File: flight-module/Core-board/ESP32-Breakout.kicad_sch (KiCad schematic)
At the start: 14 parts, among them J3 USB_B_Micro, SW1 SW_MEC_5E, SW2 SW_MEC_5E, U10 ESP32-S3-WROOM-1-N16R2, U9 AZ1084-3.3

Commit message: Finished flight-core.
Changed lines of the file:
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@@
-    (stroke (width 0) (type default))
-  )
-  (wire (pts (xy 205.74 99.06) (xy 205.74 99.822))
     (stroke (width 0) (type default))
   )
@@
     )
   )
-  (symbol (lib_id "power:GND") (at 205.74 99.822 0) (mirror y) (unit 1)
-    (in_bom yes) (on_board yes) (dnp no) (fields_autoplaced)
-    (property "Reference" "#PWR01" (at 205.74 106.172 0)
-      (effects (font (size 1.27 1.27)) hide)
-    )
-    (property "Value" "GND" (at 205.74 103.9575 0)
-      (effects (font (size 1.27 1.27)))
-    )
-    (property "Footprint" "" (at 205.74 99.822 0)
-      (effects (font (size 1.27 1.27)) hide)
-    )
-    (property "Datasheet" "" (at 205.74 99.822 0)
-      (effects (font (size 1.27 1.27)) hide)
-    )
+  (symbol (lib_id "power:GND") (at 205.74 99.06 0) (mirror y) (unit 1)
+    (in_bom yes) (on_board yes) (dnp no) (fields_autoplaced)
+    (property "Reference" "#PWR01" (at 205.74 105.41 0)
+      (effects (font (size 1.27 1.27)) hide)
+    )
+    (property "Value" "GND" (at 205.74 103.1955 0)
+      (effects (font (size 1.27 1.27)))
+    )
+    (property "Footprint" "" (at 205.74 99.06 0)
+      (effects (font (size 1.27 1.27)) hide)
+    )
+    (property "Datasheet" "" (at 205.74 99.06 0)
+      (effects (font (size 1.27 1.27)) hide)
+    )

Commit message: Updated core board.
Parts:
- removed C1 (x2): 1uF, Capacitor_SMD:C_0805_2012Metric_Pad1.18x1.45mm_HandSolder, symbol Device:C
- removed SW1, SW2: SW_MEC_5E, Button_Switch_SMD:SW_SPST_TL3305A, symbol Switch:SW_MEC_5E
- added C1 (x2): 1uF, Capacitor_SMD:C_0805_2012Metric_Pad1.18x1.45mm_HandSolder, symbol Device:C
- added SW1, SW2: 1825910-6, 1825910-6:SW_1825910-6-4, symbol 1825910-6:1825910-6
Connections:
- net BOOT: now also C1.2, SW1.3, SW1.4
- net EN: now also C1.2, SW2.3, SW2.4
- net GND: now also C1.1, C1.1, SW1.1, SW1.2, SW2.1, SW2.2
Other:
- note removed: "Buttons"

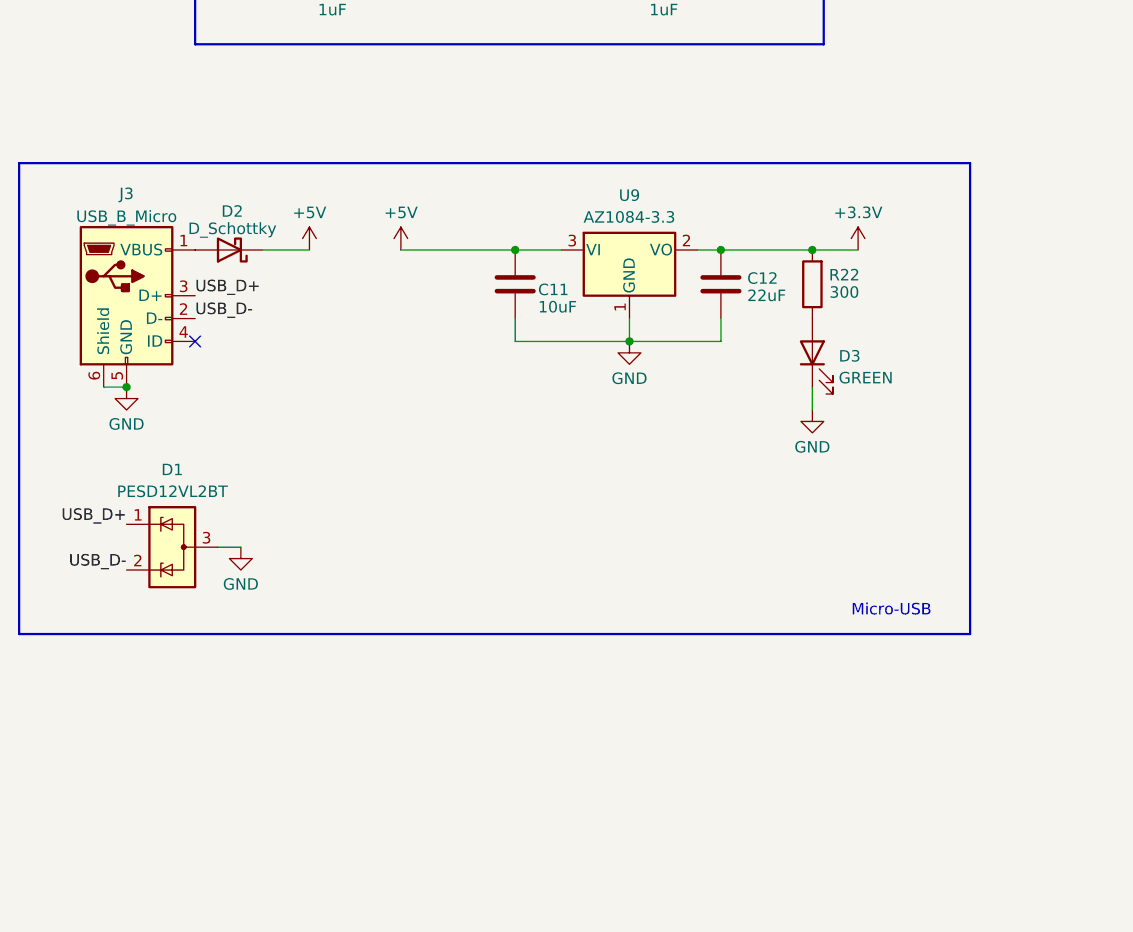
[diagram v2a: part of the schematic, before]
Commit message: Minor changes to footprint library
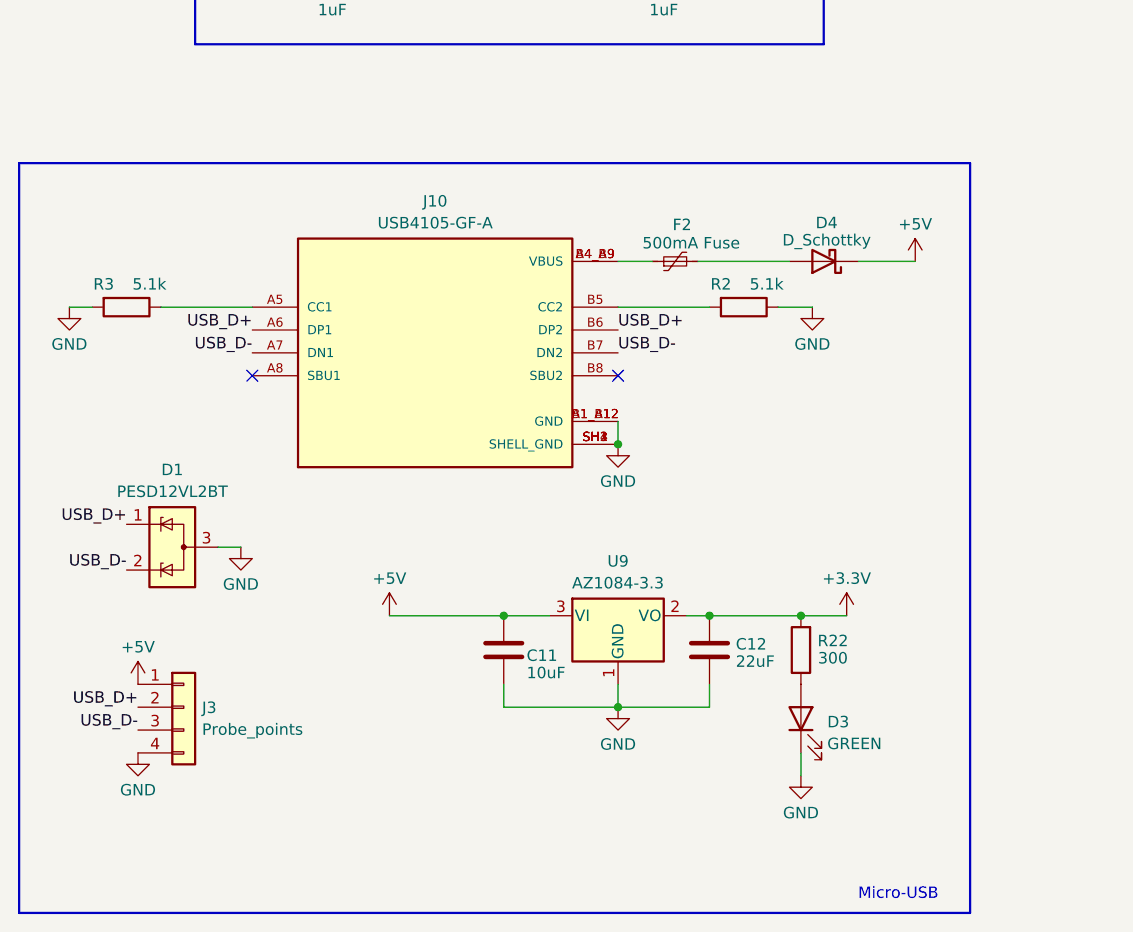
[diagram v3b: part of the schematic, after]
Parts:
- removed D2: D_Schottky, Diode_SMD:D_SOD-128, symbol Device:D_Schottky
- removed J3: USB_B_Micro, Connector_USB:USB_Micro-B_Amphenol_10103594-0001LF_Horizontal, symbol Connector:USB_B_Micro
- added D4: D_Schottky, Diode_SMD:D_SOD-128, symbol Device:D_Schottky
- added F2: 500mA Fuse, Fuse:Fuse_0603_1608Metric, symbol Device:Polyfuse_Small
- added J10: USB4105-GF-A, USB4105-GF-A:GCT_USB4105-GF-A, symbol USB4105-GF-A:USB4105-GF-A
- added J3: Probe_points, Connector_PinHeader_2.54mm:PinHeader_1x04_P2.54mm_Vertical, symbol Connector_Generic:Conn_01x04
- added R2, R3: 5.1k, Resistor_SMD:R_0805_2012Metric_Pad1.20x1.40mm_HandSolder, symbol Device:R
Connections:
- net +5V: now also D4.1 (K), J3.1 (Pin_1)
- net GND: now also J10.A1_B12 (GND), J10.B1_A12 (GND), J10.SH1 (SHELL_GND), J10.SH2 (SHELL_GND), J10.SH3 (SHELL_GND), J10.SH4 (SHELL_GND), J3.4 (Pin_4), R2.1, R3.2
- net USB_D+: now also J10.A6 (DP1), J10.B6 (DP2), J3.2 (Pin_2)
- net USB_D-: now also J10.A7 (DN1), J10.B7 (DN2), J3.3 (Pin_3)
- new net: D4.2 (A), F2.2
- new net: F2.1, J10.A4_B9 (VBUS), J10.B4_A9 (VBUS)
- new net: J10.A5 (CC1), R3.1
- new net: J10.B5 (CC2), R2.2
- no-connect marks 9 -> 10
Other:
- moved on the sheet: C11, C12, D3, R22, U9

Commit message: change the USB layout
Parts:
- J10: footprint USB4105-GF-A:GCT_USB4105-GF-A -> Connector_USB:USB_C_Receptacle_GCT_USB4105-xx-A_16P_TopMnt_Horizontal
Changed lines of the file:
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@@
       (effects (font (size 1.27 1.27)))
     )
-    (property "Footprint" "USB4105-GF-A:GCT_USB4105-GF-A" (at 80.01 100.33 0)
+    (property "Footprint" "Connector_USB:USB_C_Receptacle_GCT_USB4105-xx-A_16P_TopMnt_Horizontal" (at 80.01 100.33 0)
       (effects (font (size 1.27 1.27)) (justify bottom) hide)
     )

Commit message: in the middle of updating micro usb
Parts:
- removed D4: D_Schottky, Diode_SMD:D_SOD-128, symbol Device:D_Schottky
- removed SW1, SW2: 1825910-6, 1825910-6:SW_1825910-6-4, symbol 1825910-6:1825910-6
- added D2: D_Schottky, Diode_SMD:D_SOD-128, symbol Device:D_Schottky
- added J11: 10118194-0011LF, 10118194-0011LF:AMPHENOL_10118194-0011LF, symbol MicroUSB:10118194-0011LF
- added SW1, SW3: SW_SPST, Button_Switch_THT:SW_PUSH_6mm, symbol Switch:SW_SPST
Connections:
- net +5V: now also D2.2 (A)
- net BOOT: now also SW3.2 (B)
- net EN: now also SW1.2 (B)
- net GND: now also SW1.1 (A), SW3.1 (A)
- net USB_D+: now also J11.3 (D+); no longer J10.B6 (DP2)
- net USB_D-: now also J11.2 (D-); no longer J10.B7 (DN2)
- net at F2.2: now also J11.1 (VBUS)
- net at J10.A4_B9 (VBUS), J10.B4_A9 (VBUS): no longer F2.1
- new net: D2.1 (K), F2.1
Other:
- moved on the sheet: C11, C12, D1, D3, J10, J3, R2, R22, R3, U9

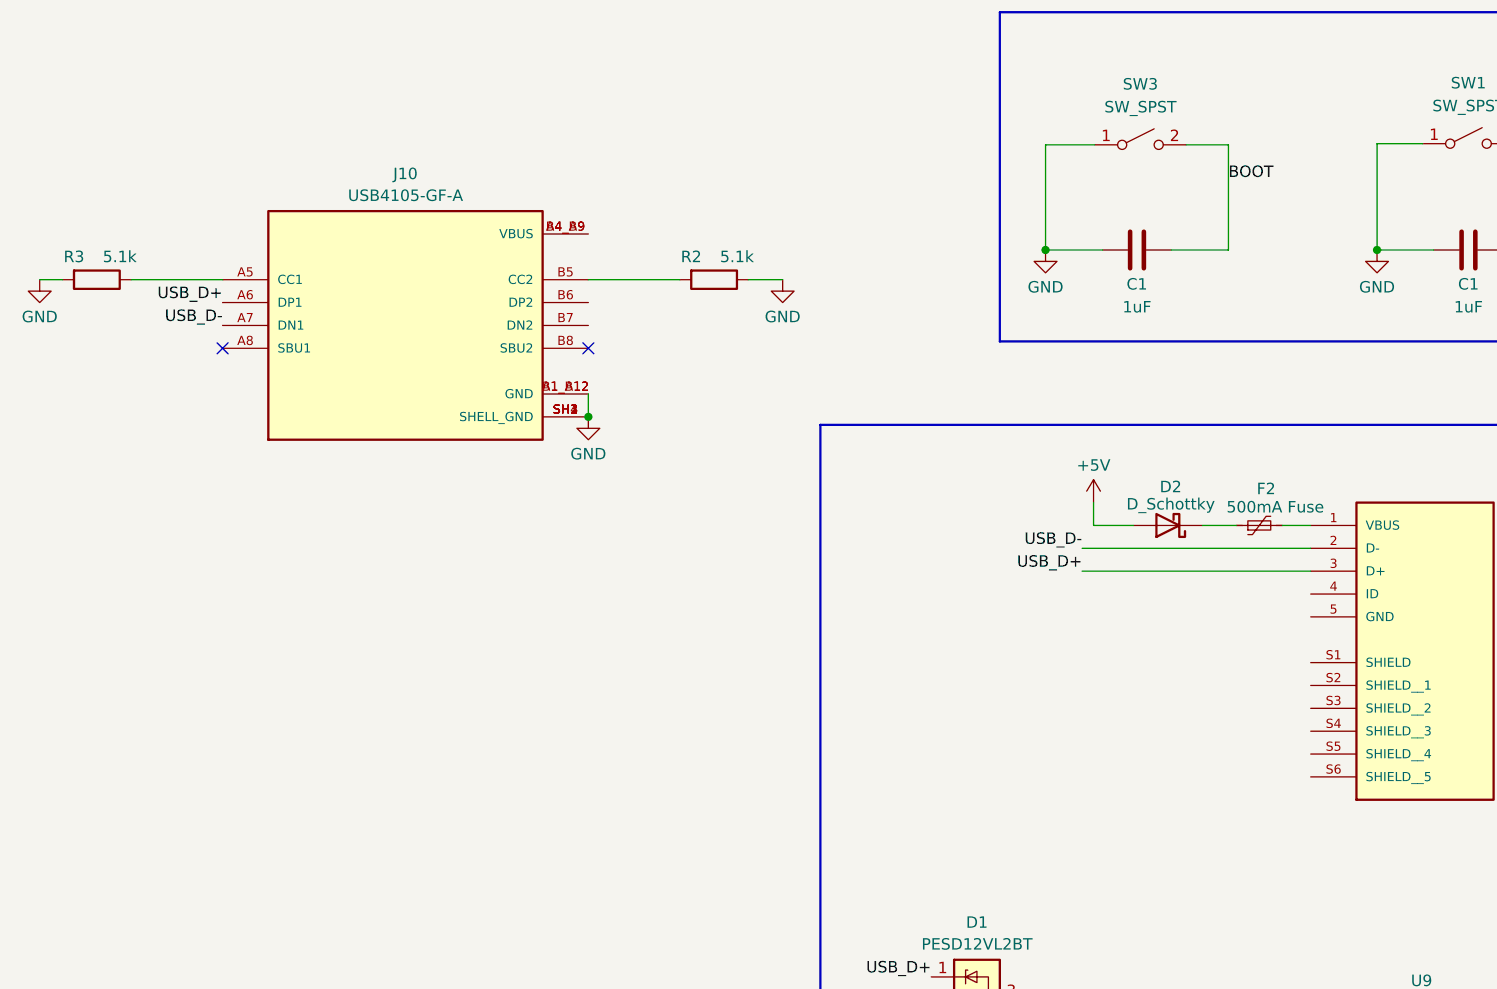
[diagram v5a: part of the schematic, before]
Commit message: still updating micro usb
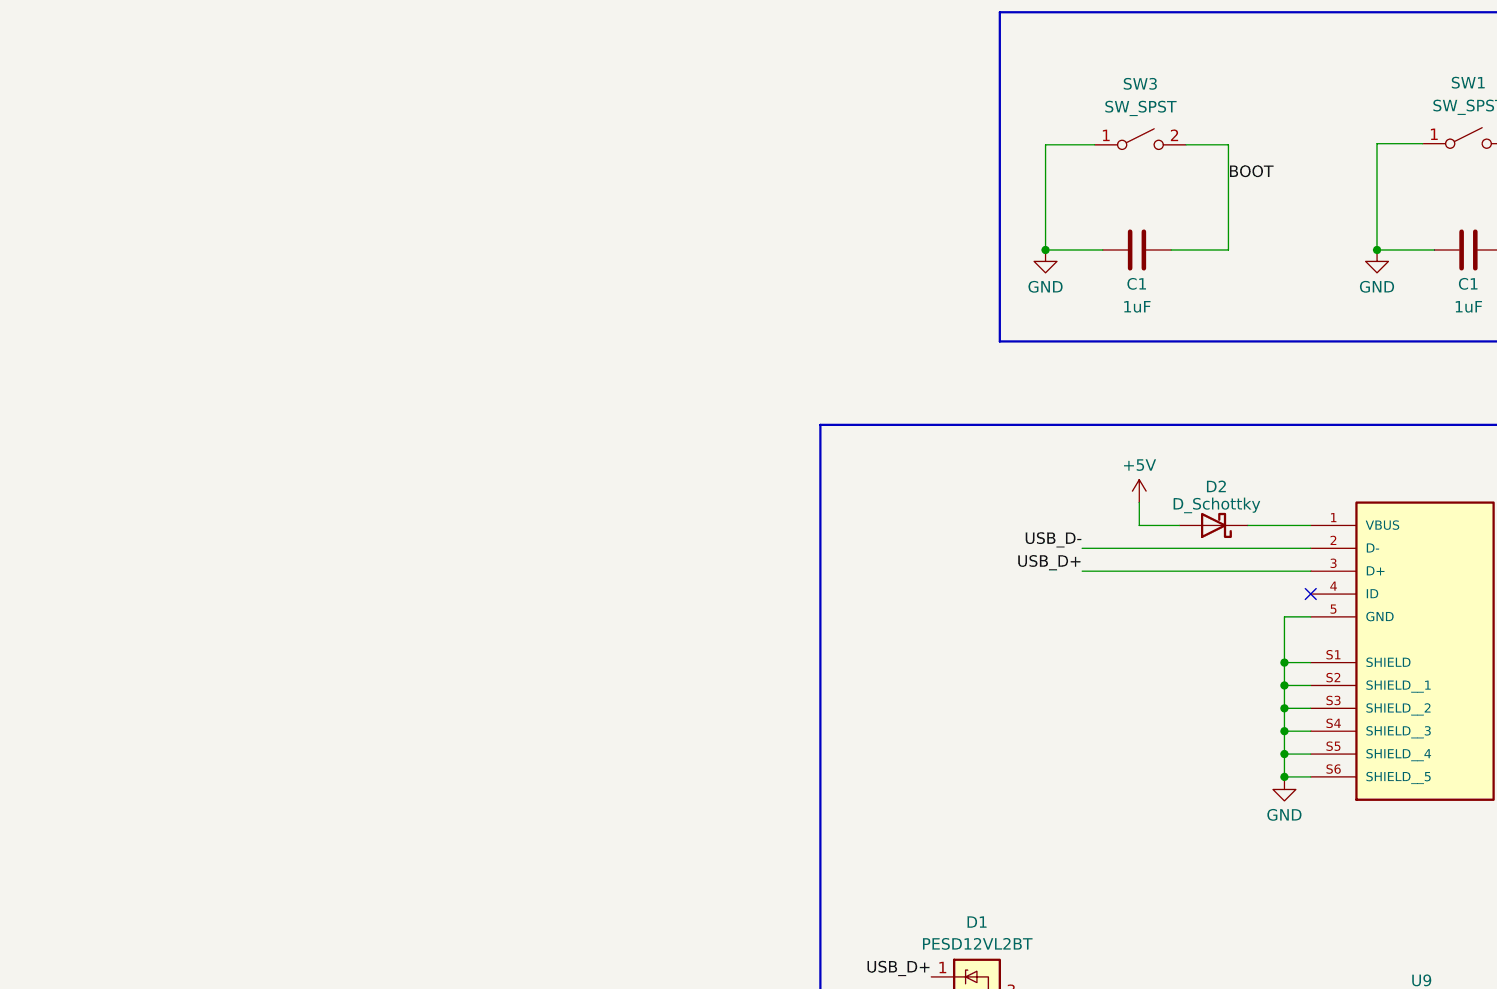
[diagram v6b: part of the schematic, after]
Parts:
- removed F2: 500mA Fuse, Fuse:Fuse_0603_1608Metric, symbol Device:Polyfuse_Small
- removed J10: USB4105-GF-A, Connector_USB:USB_C_Receptacle_GCT_USB4105-xx-A_16P_TopMnt_Horizontal, symbol USB4105-GF-A:USB4105-GF-A
- removed R2, R3: 5.1k, Resistor_SMD:R_0805_2012Metric_Pad1.20x1.40mm_HandSolder, symbol Device:R
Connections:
- net GND: now also J11.5 (GND), J11.S1 (SHIELD), J11.S2 (SHIELD__1), J11.S3 (SHIELD__2), J11.S4 (SHIELD__3), J11.S5 (SHIELD__4), J11.S6 (SHIELD__5)
- net at J11.1 (VBUS): now also D2.1 (K)
- no-connect marks 10 -> 9
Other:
- moved on the sheet: D2

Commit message: ON GOD ITS DONE
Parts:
- removed SW1, SW3: SW_SPST, Button_Switch_THT:SW_PUSH_6mm, symbol Switch:SW_SPST
- added SW1, SW2: 1825910-6, 1825910-6:SW_1825910-6-4, symbol 1825910-6:1825910-6
- J11: footprint 10118194-0011LF:AMPHENOL_10118194-0011LF -> MicroUSB:AMPHENOL_10118194-0011LF
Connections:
- net BOOT: now also SW2.3, SW2.4
- net EN: now also SW1.3, SW1.4
- net GND: now also SW1.1, SW1.2, SW2.1, SW2.2
